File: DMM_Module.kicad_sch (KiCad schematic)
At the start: 10 parts, among them J2 M20-7810245, J3 M20-7812045, J4 M20-7812045

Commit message: preliminary placement
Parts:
- removed J2 (x4): M20-7810245, bynet_Connectors:Header_SKT_02x02_Fixed_Harwin_M20-7810245, symbol Connector_Generic:Conn_02x02_Odd_Even
- removed J3: M20-7812045, bynet_Connectors:Header_SKT_02x20_Fixed_Harwin_M20-7812045, symbol MUX_Board_Interface:MCU_Board_J3
- removed J4: M20-7812045, bynet_Connectors:Header_SKT_02x20_Fixed_Harwin_M20-7812045, symbol MUX_Board_Interface:MCU_Board_J4
- MH1, MH2, MH3, MH4: symbol Mechanical:MountingHole -> sesa_mech:mh_m2.5np
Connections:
- no-connect marks 60 -> 0
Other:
- added sheet DMM DAQ (dmm_daq.kicad_sch)
- added sheet Interface (interface.kicad_sch)
- added sheet Power (power.kicad_sch)
- company: (none) -> Sesa Design Inc
- title: (none) -> ${PART_NAME}

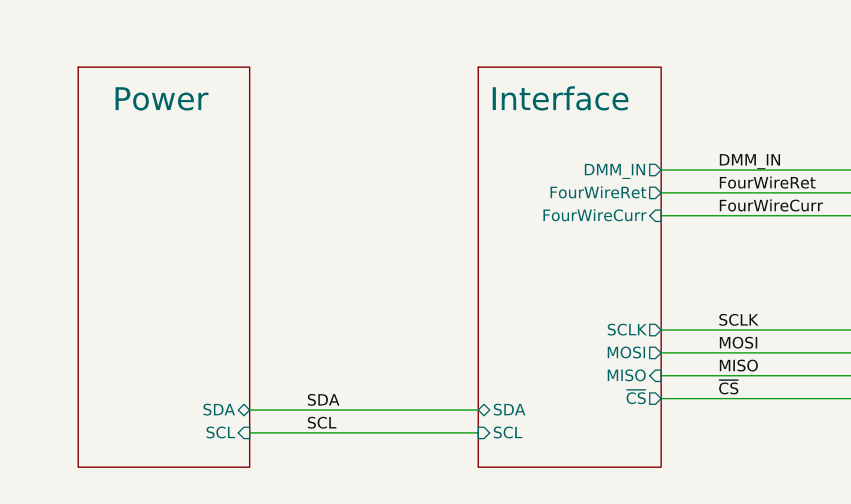
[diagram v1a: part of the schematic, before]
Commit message: Added galvanic isolation
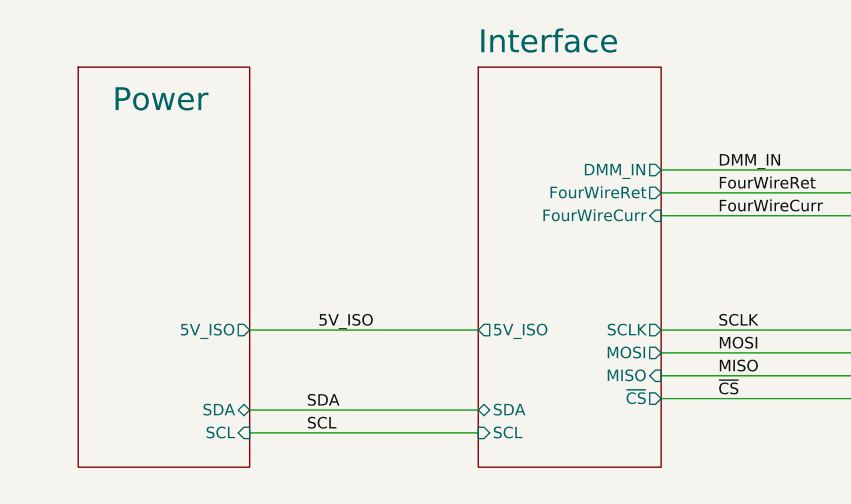
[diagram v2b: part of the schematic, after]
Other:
- sheet Interface ports: added 5V_ISO; removed none
- sheet Power ports: added 5V_ISO; removed none
